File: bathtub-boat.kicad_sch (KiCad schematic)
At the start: 23 parts, among them J1 I2C, J2 SPI, J3 I2C, J4 DS18B20, SW1 MODE, SW2 RESET, SW3 POWER, SW4 A, U1 esp-01m, U2 tp4056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

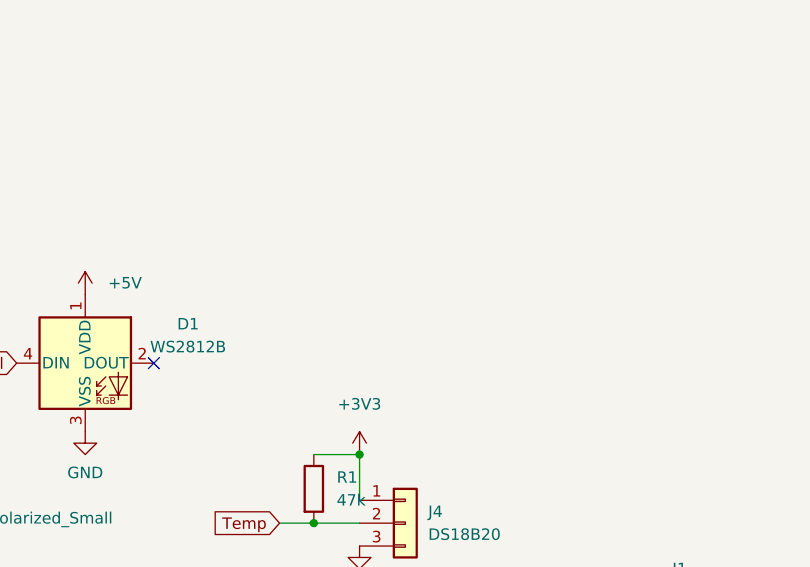
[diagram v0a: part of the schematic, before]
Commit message: Round corners some silkscreen cleanup and a TRS Plug for the 1Wire connection
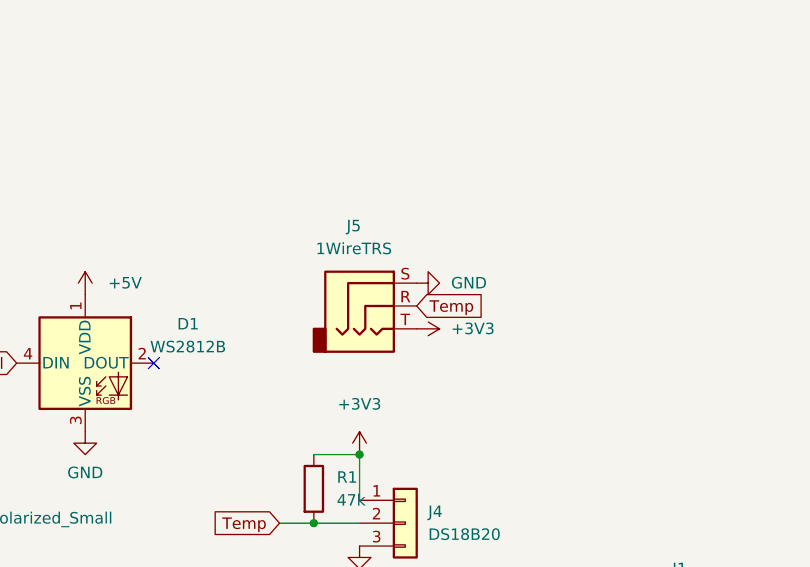
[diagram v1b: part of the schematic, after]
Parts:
- added J5: 1WireTRS, Connector_Audio:Jack_3.5mm_CUI_SJ-3523-SMT_Horizontal, symbol Connector_Audio:AudioJack3
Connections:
- net +3V3: now also J5.T
- net GND: now also J5.S
- net Temp: now also J5.R
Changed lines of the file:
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@@
+    )
+  )
+  (global_label "Temp" (shape input) (at 207.01 46.99 0) (fields_autoplaced)
+    (effects (font (size 1.27 1.27)) (justify left))
+    (property "Intersheetrefs" "${INTERSHEET_REFS}" (at 214.8937 46.99 0)
+      (effects (font (size 1.27 1.27)) (justify left) hide)
     )
   )
@@
     )
   )
+  (symbol (lib_id "power:GND") (at 207.01 44.45 90) (mirror x) (unit 1)
+    (in_bom yes) (on_board yes) (dnp no) (fields_autoplaced)
+    (property "Reference" "#PWR02" (at 213.36 44.45 0)
+      (effects (font (size 1.27 1.27)) hide)
+    )
+    (property "Value" "GND" (at 210.82 44.45 90)
+      (effects (font (size 1.27 1.27)) (justify right))
+    )
+    (property "Footprint" "" (at 207.01 44.45 0)
+      (effects (font (size 1.27 1.27)) hide)
+    )
+    (property "Datasheet" "" (at 207.01 44.45 0)
+      (effects (font (size 1.27 1.27)) hide)
+    )
+    (pin "1")
+    (instances
+      (project "bathtub-boat"
+        (path "/d50afe49-2e50-4685-b8a6-e43e950be1b7"
+          (reference "#PWR02") (unit 1)
+        )
+      )
+    )
+  )
   (symbol (lib_id "power:GND") (at 200.66 73.66 0) (mirror y) (unit 1)
     (in_bom yes) (on_board yes) (dnp no) (fields_autoplaced)
@@
     )
   )
+  (symbol (lib_id "power:+3V3") (at 207.01 49.53 270) (mirror x) (unit 1)
+    (in_bom yes) (on_board yes) (dnp no) (fields_autoplaced)
+    (property "Reference" "#PWR01" (at 203.2 49.53 0)
+      (effects (font (size 1.27 1.27)) hide)
+    )
+    (property "Value" "+3V3" (at 210.82 49.53 90)
+      (effects (font (size 1.27 1.27)) (justify left))
+    )
+    (property "Footprint" "" (at 207.01 49.53 0)
+      (effects (font (size 1.27 1.27)) hide)
+    )
+    (property "Datasheet" "" (at 207.01 49.53 0)
+      (effects (font (size 1.27 1.27)) hide)
+    )
+    (pin "1")
+    (instances
+      (project "bathtub-boat"
+        (path "/d50afe49-2e50-4685-b8a6-e43e950be1b7"
+          (reference "#PWR01") (unit 1)
+        )
+      )
+    )
+  )
   (symbol (lib_id "Switch:SW_Push") (at 180.34 109.22 0) (mirror y) (unit 1)
     (in_bom yes) (on_board yes) (dnp no)
@@
         )
       )
+    )
+  )
+  (symbol (lib_id "Connector_Audio:AudioJack3") (at 201.93 46.99 0) (unit 1)
+    (in_bom yes) (on_board yes) (dnp no) (fields_autoplaced)
+    (property "Reference" "J5" (at 200.025 38.1 0)
+      (effects (font (size 1.27 1.27)))
+    )
+    (property "Value" "1WireTRS" (at 200.025 40.64 0)
+      (effects (font (size 1.27 1.27)))
+    )
+    (property "Footprint" "Connector_Audio:Jack_3.5mm_CUI_SJ-3523-SMT_Horizontal" (at 201.93 46.99 0)
+      (effects (font (size 1.27 1.27)) hide)
+    )
+    (property "Datasheet" "~" (at 201.93 46.99 0)
+      (effects (font (size 1.27 1.27)) hide)
+    )
+    (pin "S")
+    (pin "R")
+    (pin "T")
+    (instances
+      (project "bathtub-boat"
+        (path "/d50afe49-2e50-4685-b8a6-e43e950be1b7"
+          (reference "J5") (unit 1)
+        )
+      )

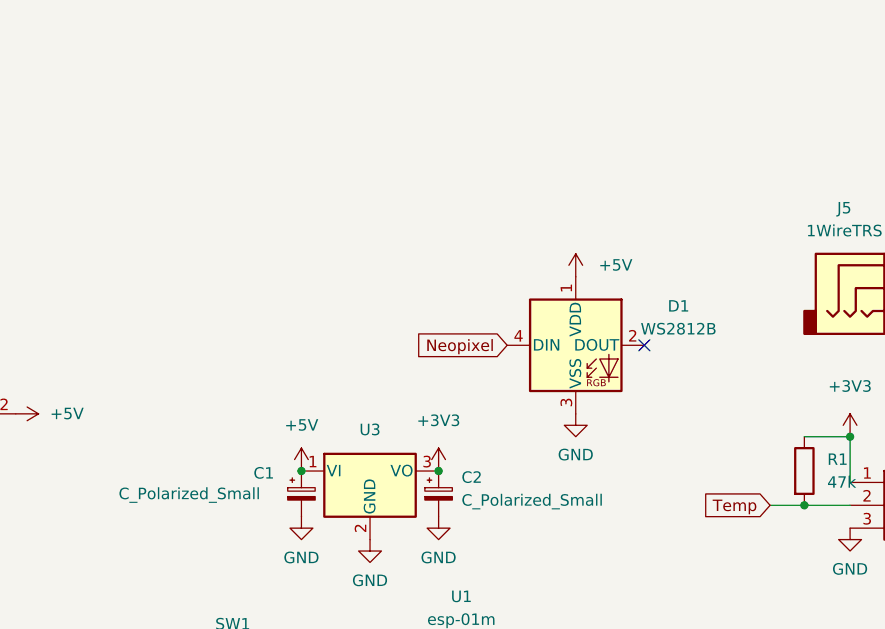
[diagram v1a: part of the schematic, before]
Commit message: Use special Play-Zone NeoPixel which has a different layout
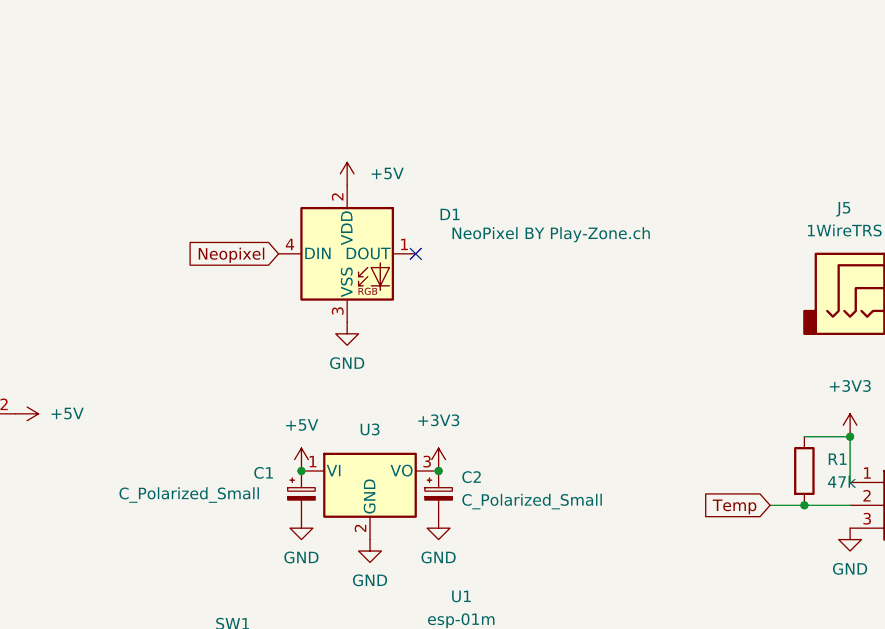
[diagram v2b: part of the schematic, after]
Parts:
- D1: value WS2812B -> NeoPixel BY Play-Zone.ch; Datasheet_alternative (none) -> https://cdn-shop.adafruit.com/datasheets/WS2812B.pdf
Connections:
- net +5V: now also D1.2 (VDD); no longer D1.1 (VDD)
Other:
- moved on the sheet: D1
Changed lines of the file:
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@@
   (junction (at 200.66 63.5) (diameter 0) (color 0 0 0 0)
   )
-  (no_connect (at 177.8 53.34))
+  (no_connect (at 152.4 43.18))
   (no_connect (at 97.79 58.42))
   (wire (pts (xy 68.58 63.5) (xy 82.55 63.5))
@@
     )
   )
-  (global_label "Neopixel" (shape input) (at 162.56 53.34 180) (fields_autoplaced)
-    (effects (font (size 1.27 1.27)) (justify right))
-    (property "Intersheetrefs" "${INTERSHEET_REFS}" (at 152.0431 53.4194 0)
+  (global_label "Neopixel" (shape input) (at 137.16 43.18 180) (fields_autoplaced)
+    (effects (font (size 1.27 1.27)) (justify right))
+    (property "Intersheetrefs" "${INTERSHEET_REFS}" (at 126.6431 43.2594 0)
       (effects (font (size 1.27 1.27)) (justify right) hide)
     )
@@
     )
   )
-  (symbol (lib_id "power:+5V") (at 170.18 45.72 0) (unit 1)
-    (in_bom yes) (on_board yes) (dnp no) (fields_autoplaced)
-    (property "Reference" "#PWR0123" (at 170.18 49.53 0)
-      (effects (font (size 1.27 1.27)) hide)
-    )
-    (property "Value" "+5V" (at 172.72 44.4499 0)
-      (effects (font (size 1.27 1.27)) (justify left))
-    )
-    (property "Footprint" "" (at 170.18 45.72 0)
-      (effects (font (size 1.27 1.27)) hide)
-    )
-    (property "Datasheet" "" (at 170.18 45.72 0)
+  (symbol (lib_id "power:+5V") (at 144.78 35.56 0) (unit 1)
+    (in_bom yes) (on_board yes) (dnp no) (fields_autoplaced)
+    (property "Reference" "#PWR0123" (at 144.78 39.37 0)
+      (effects (font (size 1.27 1.27)) hide)
+    )
+    (property "Value" "+5V" (at 147.32 34.2899 0)
+      (effects (font (size 1.27 1.27)) (justify left))
+    )
+    (property "Footprint" "" (at 144.78 35.56 0)
+      (effects (font (size 1.27 1.27)) hide)
+    )
+    (property "Datasheet" "" (at 144.78 35.56 0)
       (effects (font (size 1.27 1.27)) hide)
     )
@@
     )
   )
-  (symbol (lib_id "power:GND") (at 170.18 60.96 0) (unit 1)
-    (in_bom yes) (on_board yes) (dnp no) (fields_autoplaced)
-    (property "Reference" "#PWR0114" (at 170.18 67.31 0)
-      (effects (font (size 1.27 1.27)) hide)
-    )
-    (property "Value" "GND" (at 170.18 65.532 0)
-      (effects (font (size 1.27 1.27)))
-    )
-    (property "Footprint" "" (at 170.18 60.96 0)
-      (effects (font (size 1.27 1.27)) hide)
-    )
-    (property "Datasheet" "" (at 170.18 60.96 0)
+  (symbol (lib_id "power:GND") (at 144.78 50.8 0) (unit 1)
+    (in_bom yes) (on_board yes) (dnp no) (fields_autoplaced)
+    (property "Reference" "#PWR0114" (at 144.78 57.15 0)
+      (effects (font (size 1.27 1.27)) hide)
+    )
+    (property "Value" "GND" (at 144.78 55.372 0)
+      (effects (font (size 1.27 1.27)))
+    )
+    (property "Footprint" "" (at 144.78 50.8 0)
+      (effects (font (size 1.27 1.27)) hide)
+    )
+    (property "Datasheet" "" (at 144.78 50.8 0)
       (effects (font (size 1.27 1.27)) hide)
     )
@@
     )
   )
-  (symbol (lib_id "LED:WS2812B") (at 170.18 53.34 0) (unit 1)
-    (in_bom yes) (on_board yes) (dnp no) (fields_autoplaced)
-    (property "Reference" "D1" (at 181.61 49.0093 0)
-      (effects (font (size 1.27 1.27)))
-    )
-    (property "Value" "WS2812B" (at 181.61 51.5493 0)
-      (effects (font (size 1.27 1.27)))
-    )
-    (property "Footprint" "LED_THT:LED_D5.0mm-4_RGB_Wide_Pins" (at 171.45 60.96 0)
+  (symbol (lib_id "LED:WS2812B") (at 144.78 43.18 0) (unit 1)
+    (in_bom yes) (on_board yes) (dnp no) (fields_autoplaced)
+    (property "Reference" "D1" (at 156.21 38.8493 0)
+      (effects (font (size 1.27 1.27)))
+    )
+    (property "Value" "NeoPixel BY Play-Zone.ch" (at 167.4376 40.9448 0)
+      (effects (font (size 1.27 1.27)))
+    )
+    (property "Footprint" "LED_THT:LED_D5.0mm-4_RGB_Wide_Pins" (at 146.05 50.8 0)
       (effects (font (size 1.27 1.27)) (justify left top) hide)
     )
-    (property "Datasheet" "https://cdn-shop.adafruit.com/datasheets/WS2812B.pdf" (at 172.72 62.865 0)
+    (property "Datasheet" "https://www.play-zone.ch/de/neopixel-ws2812-diffused-5mm-through-hole-led-10-pack.html" (at 147.32 52.705 0)
       (effects (font (size 1.27 1.27)) (justify left top) hide)
     )
-    (pin "1")
+    (property "Datasheet_alternative" "https://cdn-shop.adafruit.com/datasheets/WS2812B.pdf" (at 144.78 43.18 0)
+      (effects (font (size 1.27 1.27)) hide)
+    )
+    (pin "1")

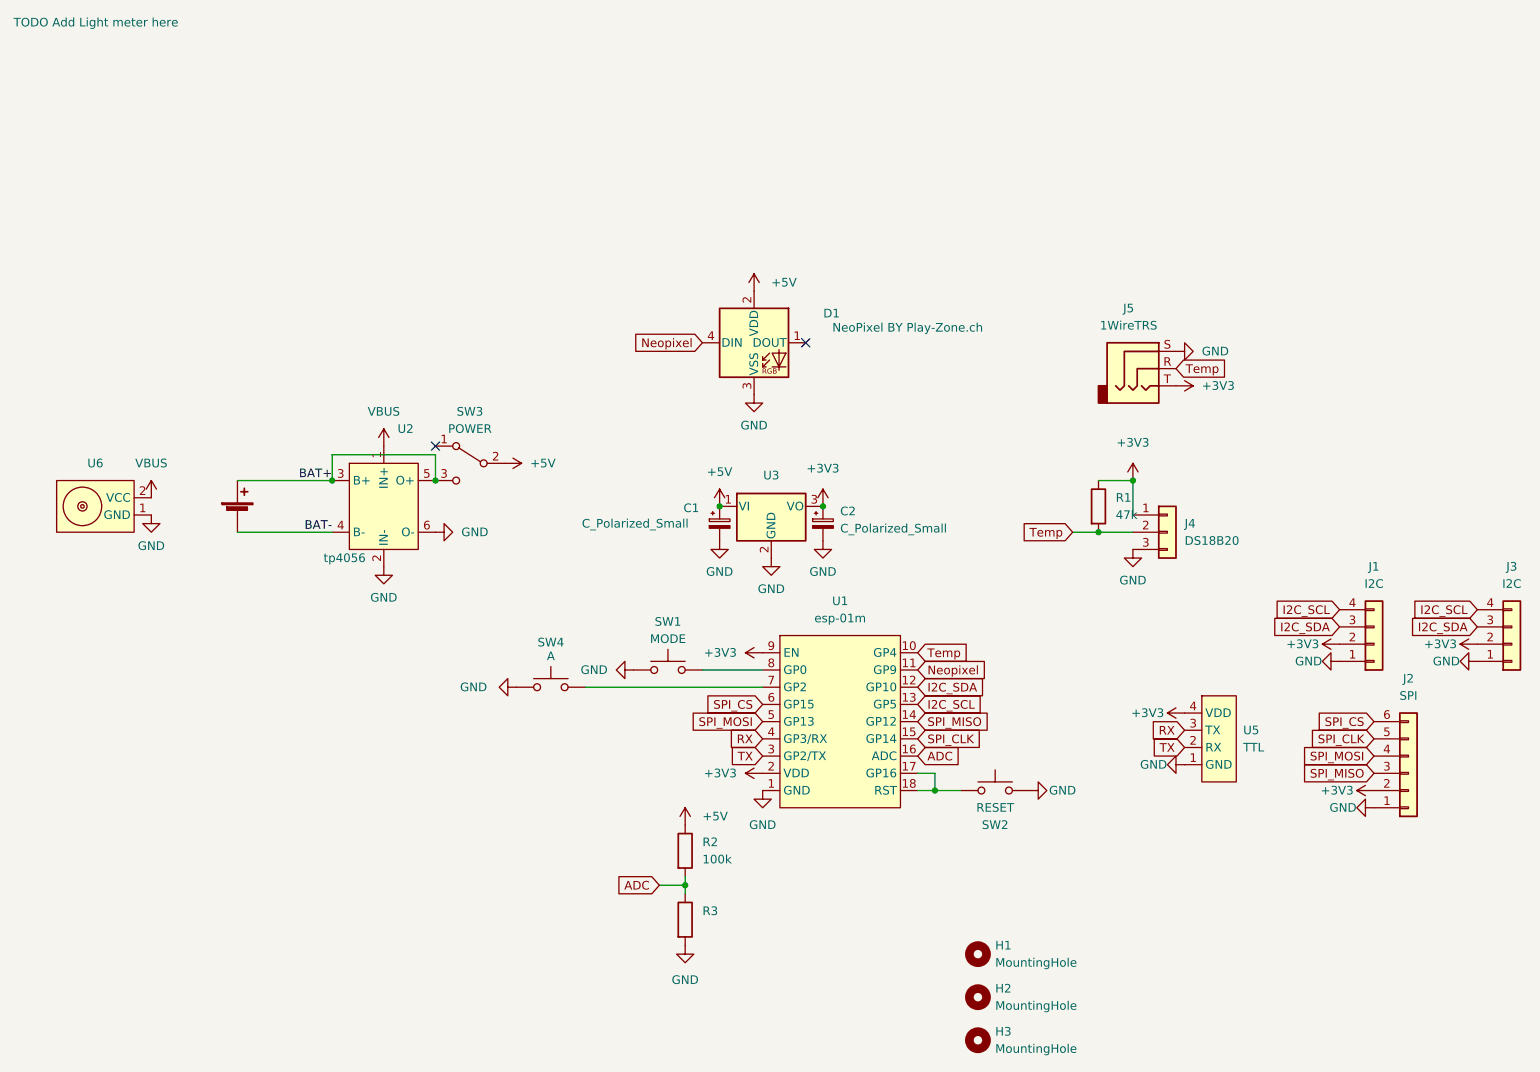
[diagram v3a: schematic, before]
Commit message: Add a DS18B20 that is facing downwards in the center for under water placement
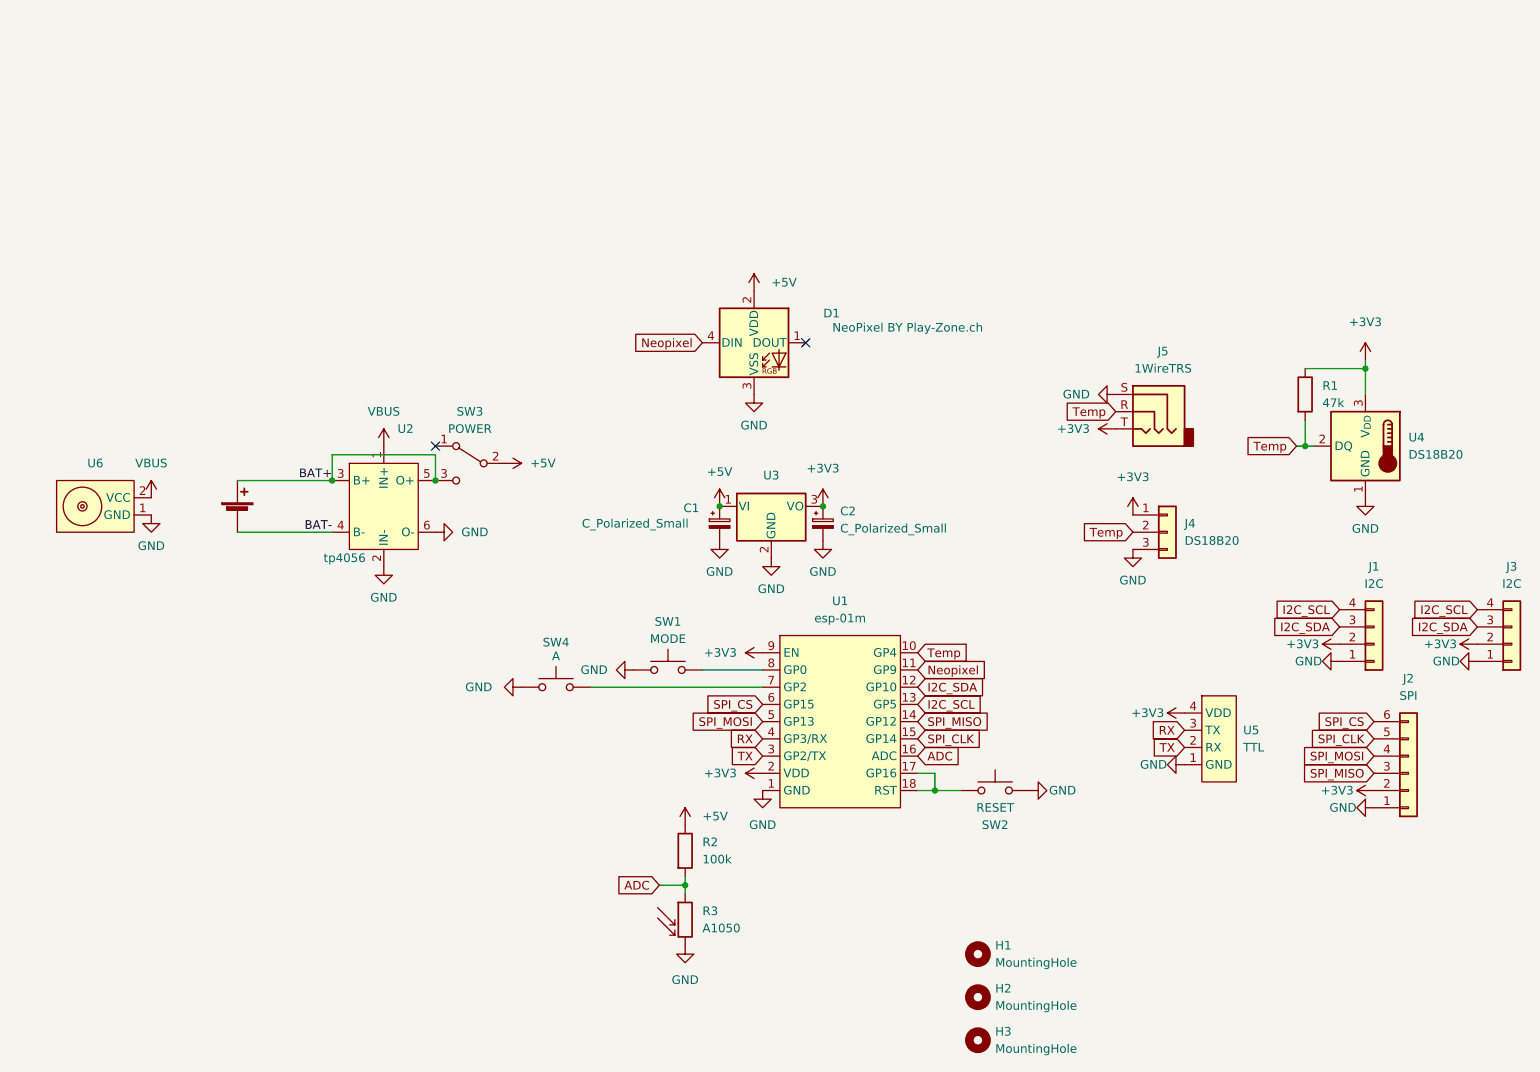
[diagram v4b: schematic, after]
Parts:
- removed R3: TODO Add Light meter here, Resistor_THT:R_Axial_DIN0204_L3.6mm_D1.6mm_P1.90mm_Vertical, symbol Device:R
- added R3: A1050, OptoDevice:R_LDR_4.9x4.2mm_P2.54mm_Vertical, symbol Sensor_Optical:A1050
- added U4: DS18B20, Package_TO_SOT_THT:TO-92_Inline, symbol Sensor_Temperature:DS18B20
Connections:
- net +3V3: now also U4.3 (V_{DD})
- net ADC: now also R3.1
- net GND: now also R3.2, U4.1 (GND)
- net Temp: now also U4.2 (DQ)
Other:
- moved on the sheet: J5, R1, SW4

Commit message: Change resistors, improve silkscreen and add OSHW logo
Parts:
- R2: footprint Resistor_THT:R_Axial_DIN0204_L3.6mm_D1.6mm_P1.90mm_Vertical -> Resistor_THT:R_Axial_DIN0207_L6.3mm_D2.5mm_P7.62mm_Horizontal
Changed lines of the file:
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@@
       (effects (font (size 1.27 1.27)) (justify left))
     )
-    (property "Footprint" "Resistor_THT:R_Axial_DIN0204_L3.6mm_D1.6mm_P1.90mm_Vertical" (at 132.842 118.11 90)
+    (property "Footprint" "Resistor_THT:R_Axial_DIN0207_L6.3mm_D2.5mm_P7.62mm_Horizontal" (at 132.842 118.11 90)
       (effects (font (size 1.27 1.27)) hide)
     )

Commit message: Final tweaks prior to production
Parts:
- R1: footprint Resistor_THT:R_Axial_DIN0204_L3.6mm_D1.6mm_P1.90mm_Vertical -> Resistor_THT:R_Axial_DIN0207_L6.3mm_D2.5mm_P7.62mm_Horizontal
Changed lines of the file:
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@@
       (effects (font (size 1.27 1.27)) (justify left))
     )
-    (property "Footprint" "Resistor_THT:R_Axial_DIN0204_L3.6mm_D1.6mm_P1.90mm_Vertical" (at 224.282 50.8 90)
+    (property "Footprint" "Resistor_THT:R_Axial_DIN0207_L6.3mm_D2.5mm_P7.62mm_Horizontal" (at 224.282 50.8 90)
       (effects (font (size 1.27 1.27)) hide)
     )
